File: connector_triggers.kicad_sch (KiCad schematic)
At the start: 3 parts

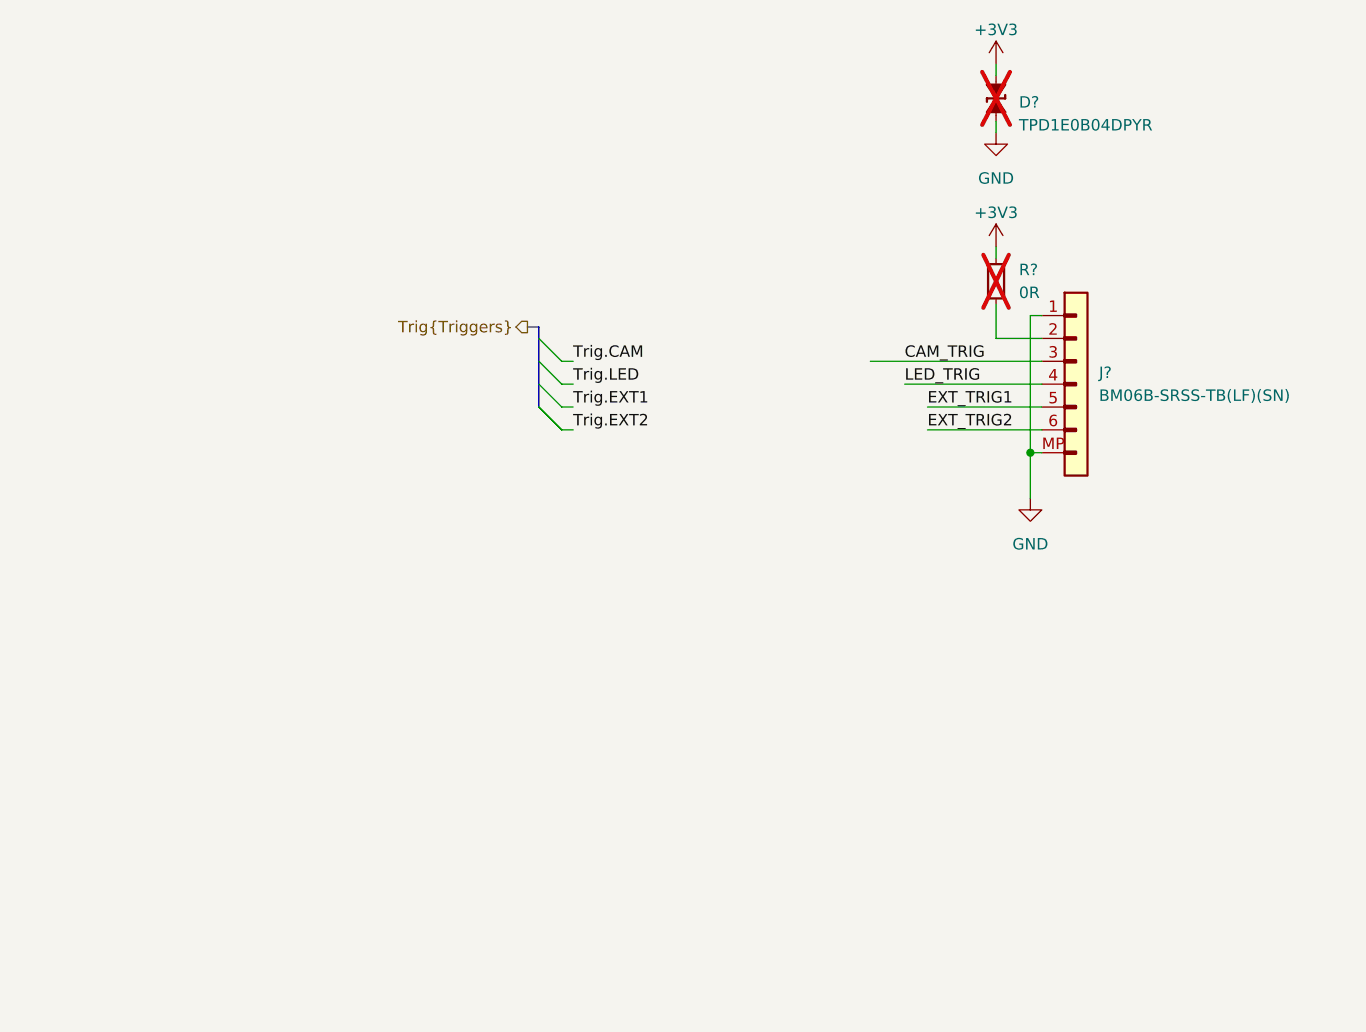
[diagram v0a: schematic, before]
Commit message: [#72133] Add protection to trigger conn
Signed-off-by: Dawid Lentka <dlentka@antmicro.com>
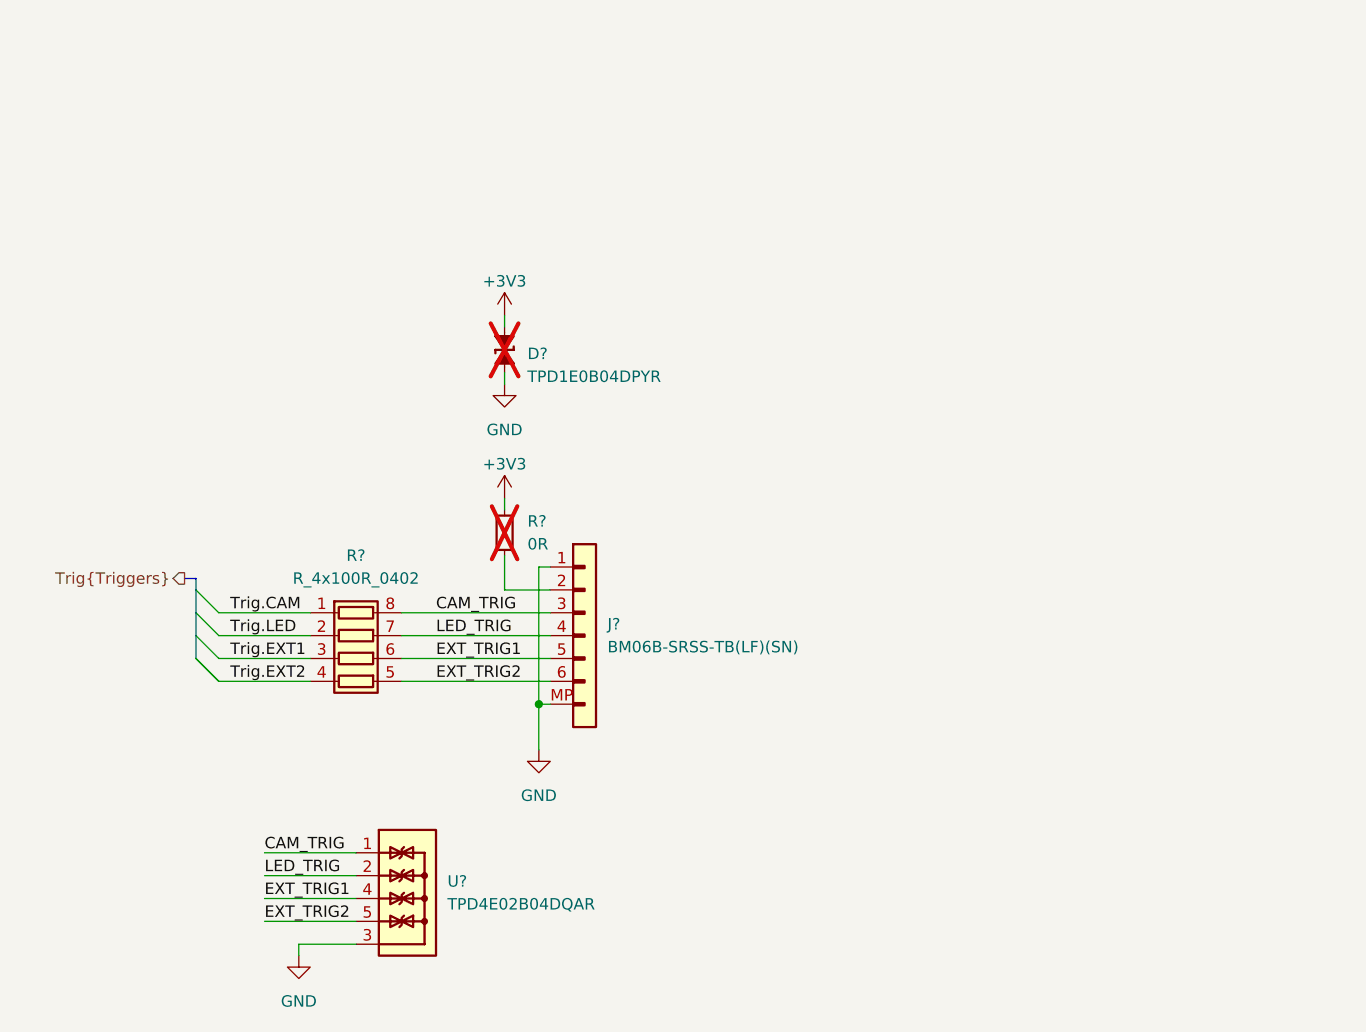
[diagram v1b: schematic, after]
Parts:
- added R?: R_4x100R_0402_array, antmicro-footprints:R_Array_4x0402_Panasonic_EXB28V, symbol antmicroResistorNetworksArrays:R_4x100R_0402_array
- added U?: TPD4E02B04DQA, antmicro-footprints:USON-10_2.5x1mm_P0.5mm, symbol antmicroTVSDiodes:TPD4E02B04DQA
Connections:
- net CAM_TRIG: now also R?.8 (R1.2), U?.1, U?.10
- net EXT_TRIG1: now also R?.6 (R3.2), U?.4, U?.7
- net EXT_TRIG2: now also R?.5 (R4.2), U?.5, U?.6
- net GND: now also U?.3, U?.8
- net LED_TRIG: now also R?.7 (R2.2), U?.2, U?.9
- net Trig.CAM: now also R?.1 (R1.1)
- net Trig.EXT1: now also R?.3 (R3.1)
- net Trig.EXT2: now also R?.4 (R4.1)
- net Trig.LED: now also R?.2 (R2.1)
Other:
- moved on the sheet: D?, J?, R?

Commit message: [#72133] Unify sheet size
Signed-off-by: Dawid Lentka <dlentka@antmicro.com>
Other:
- title: (none) -> LED Panel Board
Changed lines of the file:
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@@
 	(generator_version "8.0")
 	(paper "A4")
+	(title_block
+		(title "LED Panel Board")
+		(date "28.01.2025")
+		(rev "1.0.0")
+	)
 	(junction
 		(at 158.75 102.87)

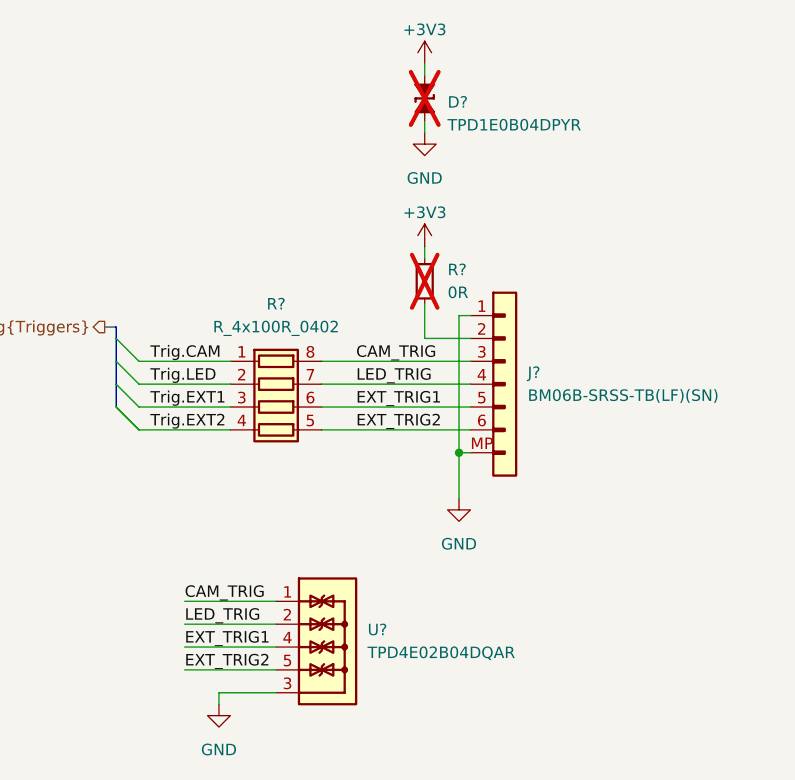
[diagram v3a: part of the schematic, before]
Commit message: [#72133] Annotate schematics
Signed-off-by: Dawid Lentka <dlentka@antmicro.com>
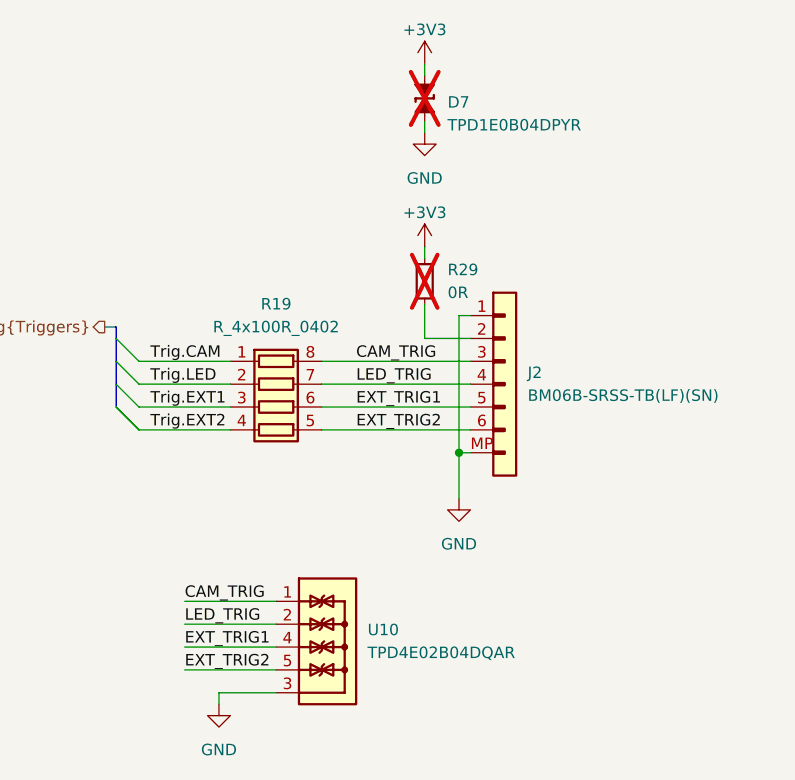
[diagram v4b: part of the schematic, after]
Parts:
- gave numbers to parts that had none: 5
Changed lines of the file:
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@@
 		(on_board yes)
 		(dnp no)
-		(property "Reference" "#PWR082"
+		(property "Reference" "#PWR0103"
 			(at 170.18 59.69 0)
 			(effects
@@
 			(project "led-panel"
 				(path "/a86e1cab-ea0a-45e6-9194-d44b0d5c9450/0f1bd089-cb15-4e08-bb57-9fcbc9174dd1"
-					(reference "#PWR082")
+					(reference "#PWR0103")
 					(unit 1)
 				)
 				(path "/a86e1cab-ea0a-45e6-9194-d44b0d5c9450/50c5f44e-0866-4019-828a-f0d4c007daad"
-					(reference "#PWR080")
+					(reference "#PWR075")
 					(unit 1)
 				)
@@
 				)
 				(path "/a86e1cab-ea0a-45e6-9194-d44b0d5c9450/50c5f44e-0866-4019-828a-f0d4c007daad"
-					(reference "#PWR0101")
+					(reference "#PWR074")
 					(unit 1)
 				)
@@
 		(dnp no)
 		(fields_autoplaced yes)
-		(property "Reference" "J?"
+		(property "Reference" "J2"
 			(at 166.37 93.98 0)
 			(effects
@@
 			(project "led-panel"
 				(path "/a86e1cab-ea0a-45e6-9194-d44b0d5c9450/0f1bd089-cb15-4e08-bb57-9fcbc9174dd1"
-					(reference "J?")
+					(reference "J2")
 					(unit 1)
 				)
 				(path "/a86e1cab-ea0a-45e6-9194-d44b0d5c9450/50c5f44e-0866-4019-828a-f0d4c007daad"
-					(reference "J?")
+					(reference "J1")
 					(unit 1)
 				)
@@
 		(dnp yes)
 		(fields_autoplaced yes)
-		(property "Reference" "D?"
+		(property "Reference" "D7"
 			(at 157.48 63.9366 90)
 			(effects
@@
 			(project "led-panel"
 				(path "/a86e1cab-ea0a-45e6-9194-d44b0d5c9450/0f1bd089-cb15-4e08-bb57-9fcbc9174dd1"
-					(reference "D?")
+					(reference "D7")
 					(unit 1)
 				)
 				(path "/a86e1cab-ea0a-45e6-9194-d44b0d5c9450/50c5f44e-0866-4019-828a-f0d4c007daad"
-					(reference "D?")
+					(reference "D5")
 					(unit 1)
 				)
@@
 		(dnp no)
 		(fields_autoplaced yes)
-		(property "Reference" "#PWR083"
+		(property "Reference" "#PWR0104"
 			(at 163.83 69.85 0)
 			(effects
@@
 			(project "led-panel"
 				(path "/a86e1cab-ea0a-45e6-9194-d44b0d5c9450/0f1bd089-cb15-4e08-bb57-9fcbc9174dd1"
-					(reference "#PWR083")
+					(reference "#PWR0104")
 					(unit 1)
 				)
 				(path "/a86e1cab-ea0a-45e6-9194-d44b0d5c9450/50c5f44e-0866-4019-828a-f0d4c007daad"
-					(reference "#PWR081")
+					(reference "#PWR076")
 					(unit 1)
 				)
@@
 		(dnp yes)
 		(fields_autoplaced yes)
-		(property "Reference" "R?"
+		(property "Reference" "R29"
 			(at 157.48 82.55 90)
 			(effects
@@
 			(project "led-panel"
 				(path "/a86e1cab-ea0a-45e6-9194-d44b0d5c9450/0f1bd089-cb15-4e08-bb57-9fcbc9174dd1"
-					(reference "R?")
+					(reference "R29")
 					(unit 1)
 				)
 				(path "/a86e1cab-ea0a-45e6-9194-d44b0d5c9450/50c5f44e-0866-4019-828a-f0d4c007daad"
-					(reference "R?")
+					(reference "R20")
 					(unit 1)
 				)
@@
 		(dnp no)
 		(fields_autoplaced yes)
-		(property "Reference" "U?"
+		(property "Reference" "U10"
 			(at 148.59 122.555 0)
 			(effects
@@
 			(project "led-panel"
 				(path "/a86e1cab-ea0a-45e6-9194-d44b0d5c9450/0f1bd089-cb15-4e08-bb57-9fcbc9174dd1"
-					(reference "U?")
+					(reference "U10")
 					(unit 1)
 				)
 				(path "/a86e1cab-ea0a-45e6-9194-d44b0d5c9450/50c5f44e-0866-4019-828a-f0d4c007daad"
-					(reference "U?")
+					(reference "U7")
 					(unit 1)
 				)
@@
 		(on_board yes)
 		(dnp no)
-		(property "Reference" "#PWR051"
+		(property "Reference" "#PWR0105"
 			(at 170.18 80.01 0)
 			(effects
@@
 			(project "led-panel"
 				(path "/a86e1cab-ea0a-45e6-9194-d44b0d5c9450/0f1bd089-cb15-4e08-bb57-9fcbc9174dd1"
-					(reference "#PWR051")
+					(reference "#PWR0105")
 					(unit 1)
 				)
 				(path "/a86e1cab-ea0a-45e6-9194-d44b0d5c9450/50c5f44e-0866-4019-828a-f0d4c007daad"
-					(reference "#PWR049")
+					(reference "#PWR077")
 					(unit 1)
 				)
@@
 		(dnp no)
 		(fields_autoplaced yes)
-		(property "Reference" "R?"
+		(property "Reference" "R19"
 			(at 138.43 86.36 0)
 			(effects
@@
 			(project "led-panel"
 				(path "/a86e1cab-ea0a-45e6-9194-d44b0d5c9450/0f1bd089-cb15-4e08-bb57-9fcbc9174dd1"
-					(reference "R?")
+					(reference "R28")
 					(unit 1)
 				)
 				(path "/a86e1cab-ea0a-45e6-9194-d44b0d5c9450/50c5f44e-0866-4019-828a-f0d4c007daad"
-					(reference "R?")
+					(reference "R19")
 					(unit 1)
 				)
@@
 		(dnp no)
 		(fields_autoplaced yes)
-		(property "Reference" "#PWR052"
+		(property "Reference" "#PWR0106"
 			(at 167.64 110.49 0)
 			(effects
@@
 			(project "led-panel"
 				(path "/a86e1cab-ea0a-45e6-9194-d44b0d5c9450/0f1bd089-cb15-4e08-bb57-9fcbc9174dd1"
-					(reference "#PWR052")
+					(reference "#PWR0106")
 					(unit 1)
 				)
 				(path "/a86e1cab-ea0a-45e6-9194-d44b0d5c9450/50c5f44e-0866-4019-828a-f0d4c007daad"
-					(reference "#PWR050")
-					(unit 1)
-				)
+					(reference "#PWR078")
+					(unit 1)
+				)

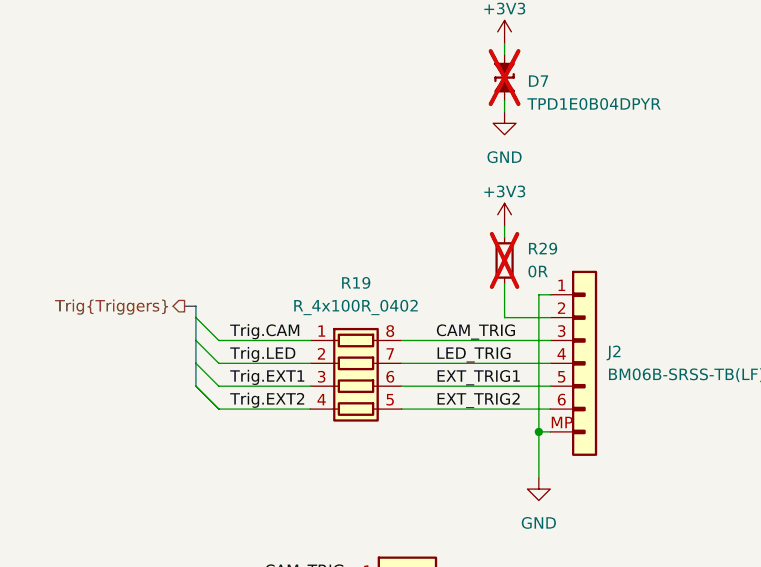
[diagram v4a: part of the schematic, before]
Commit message: [#72133] Clean ERC
Signed-off-by: Dawid Lentka <dlentka@antmicro.com>
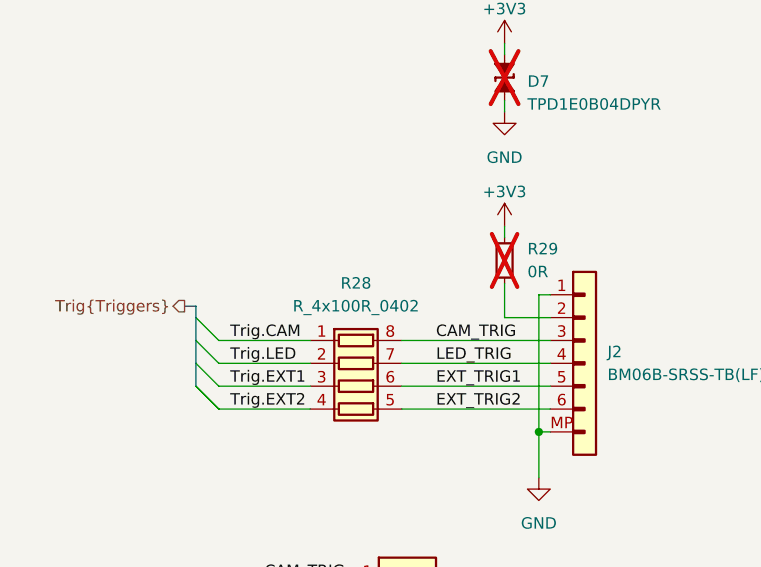
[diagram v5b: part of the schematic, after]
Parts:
- renumbered R19 to R28
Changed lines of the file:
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@@
 		(dnp no)
 		(fields_autoplaced yes)
-		(property "Reference" "R19"
+		(property "Reference" "R28"
 			(at 138.43 86.36 0)
 			(effects

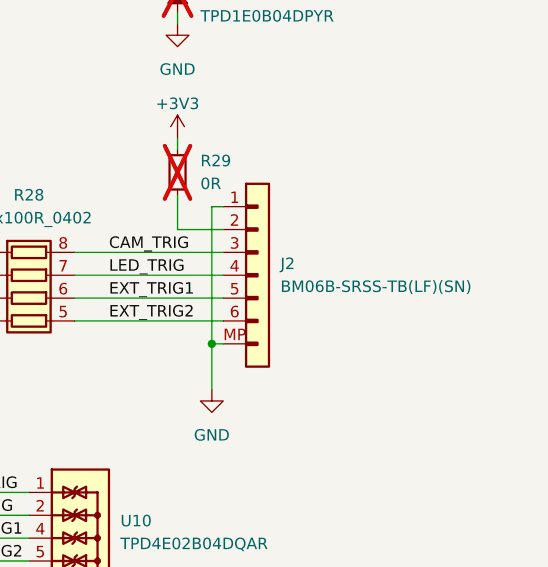
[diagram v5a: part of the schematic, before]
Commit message: [#72133] Change connectors to horizontal
Signed-off-by: Dawid Lentka <dlentka@antmicro.com>
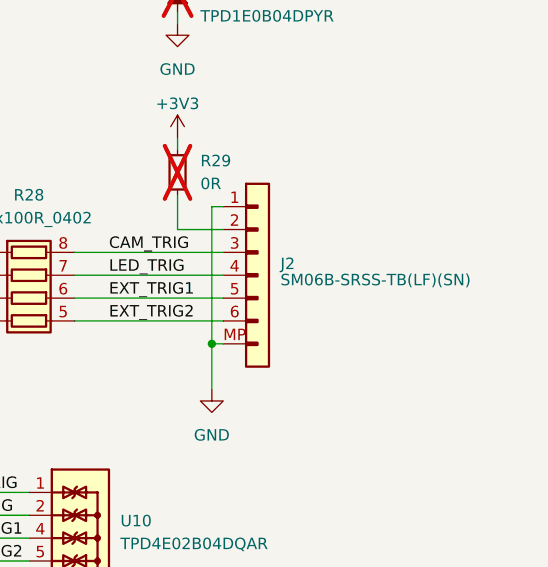
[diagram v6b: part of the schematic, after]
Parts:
- J2: value JST_SH_1x6_BM06B-SRSS-TB-LF-SN -> JST_SH_1x6_SM06B-SRSS-TB-LF-SN; footprint antmicro-footprints:Conn_JST_SH_1x6_BM06B-SRSS-TB-LF-SN -> antmicro-footprints:Conn_JST_SH_1x6_SM06B-SRSS-TB-LF-SN; symbol antmicroWire2BoardConnectors:JST_SH_1x6_BM06B-SRSS-TB-LF-SN -> antmicroWire2BoardConnectors:JST_SH_1x6_SM06B-SRSS-TB-LF-SN; MPN BM06B-SRSS-TB(LF)(SN) -> SM06B-SRSS-TB(LF)(SN)
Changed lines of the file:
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@@
 	)
 	(symbol
-		(lib_id "antmicroWire2BoardConnectors:JST_SH_1x6_BM06B-SRSS-TB-LF-SN")
+		(lib_id "antmicroWire2BoardConnectors:JST_SH_1x6_SM06B-SRSS-TB-LF-SN")
 		(at 160.02 87.63 0)
 		(unit 1)
@@
 			)
 		)
-		(property "Value" "JST_SH_1x6_BM06B-SRSS-TB-LF-SN"
+		(property "Value" "JST_SH_1x6_SM06B-SRSS-TB-LF-SN"
 			(at 180.34 95.25 0)
 			(effects
@@
 			)
 		)
-		(property "Footprint" "antmicro-footprints:Conn_JST_SH_1x6_BM06B-SRSS-TB-LF-SN"
+		(property "Footprint" "antmicro-footprints:Conn_JST_SH_1x6_SM06B-SRSS-TB-LF-SN"
 			(at 180.34 97.79 0)
 			(effects
@@
 			)
 		)
-		(property "Datasheet" "https://www.farnell.com/datasheets/2082363.pdf"
+		(property "Datasheet" "https://www.jst-mfg.com/product/pdf/eng/eSH.pdf"
 			(at 180.34 100.33 0)
 			(effects
@@
 			)
 		)
-		(property "Description" "Pin Header, Vertical, Wire-to-Board, 1 mm, 1 Rows, 6 Contacts, Surface Mount Straight, SH"
+		(property "Description" "Pin Header, Right Angle, Wire-to-Board, 1 mm, 1 Rows, 6 Contacts, Surface Mount Right Angle, SR"
 			(at 160.02 87.63 0)
 			(effects
@@
 			)
 		)
-		(property "MPN" "BM06B-SRSS-TB(LF)(SN)"
+		(property "MPN" "SM06B-SRSS-TB(LF)(SN)"
 			(at 166.37 96.52 0)
 			(effects
@@
 					(thickness 0.15)
 				)
-				(justify left)
+				(justify left bottom)
 			)
 		)

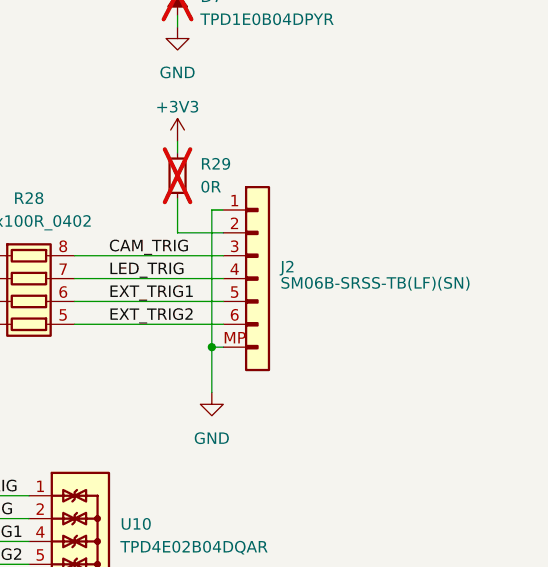
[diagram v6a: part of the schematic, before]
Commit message: [#72133] Sch: Update control hierarchy
Signed-off-by: Dawid Lentka <dlentka@antmicro.com>
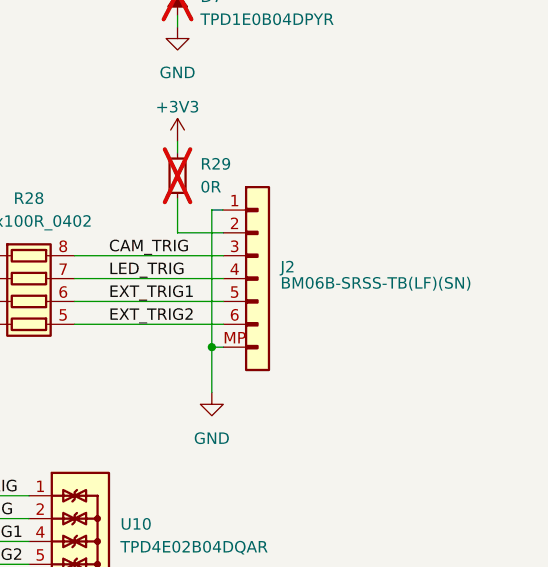
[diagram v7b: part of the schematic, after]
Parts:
- J2: value JST_SH_1x6_SM06B-SRSS-TB-LF-SN -> JST_SH_1x6_BM06B-SRSS-TB-LF-SN; footprint antmicro-footprints:Conn_JST_SH_1x6_SM06B-SRSS-TB-LF-SN -> antmicro-footprints:Conn_JST_SH_1x6_BM06B-SRSS-TB-LF-SN; symbol antmicroWire2BoardConnectors:JST_SH_1x6_SM06B-SRSS-TB-LF-SN -> antmicroWire2BoardConnectors:JST_SH_1x6_BM06B-SRSS-TB-LF-SN; MPN SM06B-SRSS-TB(LF)(SN) -> BM06B-SRSS-TB(LF)(SN)
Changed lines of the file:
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@@
 	)
 	(symbol
-		(lib_id "antmicroWire2BoardConnectors:JST_SH_1x6_SM06B-SRSS-TB-LF-SN")
+		(lib_id "antmicroWire2BoardConnectors:JST_SH_1x6_BM06B-SRSS-TB-LF-SN")
 		(at 160.02 87.63 0)
 		(unit 1)
@@
 			)
 		)
-		(property "Value" "JST_SH_1x6_SM06B-SRSS-TB-LF-SN"
+		(property "Value" "JST_SH_1x6_BM06B-SRSS-TB-LF-SN"
 			(at 180.34 95.25 0)
 			(effects
@@
 			)
 		)
-		(property "Footprint" "antmicro-footprints:Conn_JST_SH_1x6_SM06B-SRSS-TB-LF-SN"
+		(property "Footprint" "antmicro-footprints:Conn_JST_SH_1x6_BM06B-SRSS-TB-LF-SN"
 			(at 180.34 97.79 0)
 			(effects
@@
 			)
 		)
-		(property "Datasheet" "https://www.jst-mfg.com/product/pdf/eng/eSH.pdf"
+		(property "Datasheet" "https://www.farnell.com/datasheets/2082363.pdf"
 			(at 180.34 100.33 0)
 			(effects
@@
 			)
 		)
-		(property "Description" "Pin Header, Right Angle, Wire-to-Board, 1 mm, 1 Rows, 6 Contacts, Surface Mount Right Angle, SR"
+		(property "Description" "Pin Header, Vertical, Wire-to-Board, 1 mm, 1 Rows, 6 Contacts, Surface Mount Straight, SH"
 			(at 160.02 87.63 0)
 			(effects
@@
 			)
 		)
-		(property "MPN" "SM06B-SRSS-TB(LF)(SN)"
+		(property "MPN" "BM06B-SRSS-TB(LF)(SN)"
 			(at 166.37 96.52 0)
 			(effects
